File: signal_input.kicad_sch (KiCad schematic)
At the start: 48 parts, among them IC1 TXU0104QWBQARQ1, IC2 TXU0104QWBQARQ1, IC3 TXU0104QWBQARQ1, IC4 TXU0104QWBQARQ1, J4 6101XX249121_610108249121, J5 6101XX249121_610108249121, J6 6101XX249121_610108249121, J7 6101XX249121_610108249121

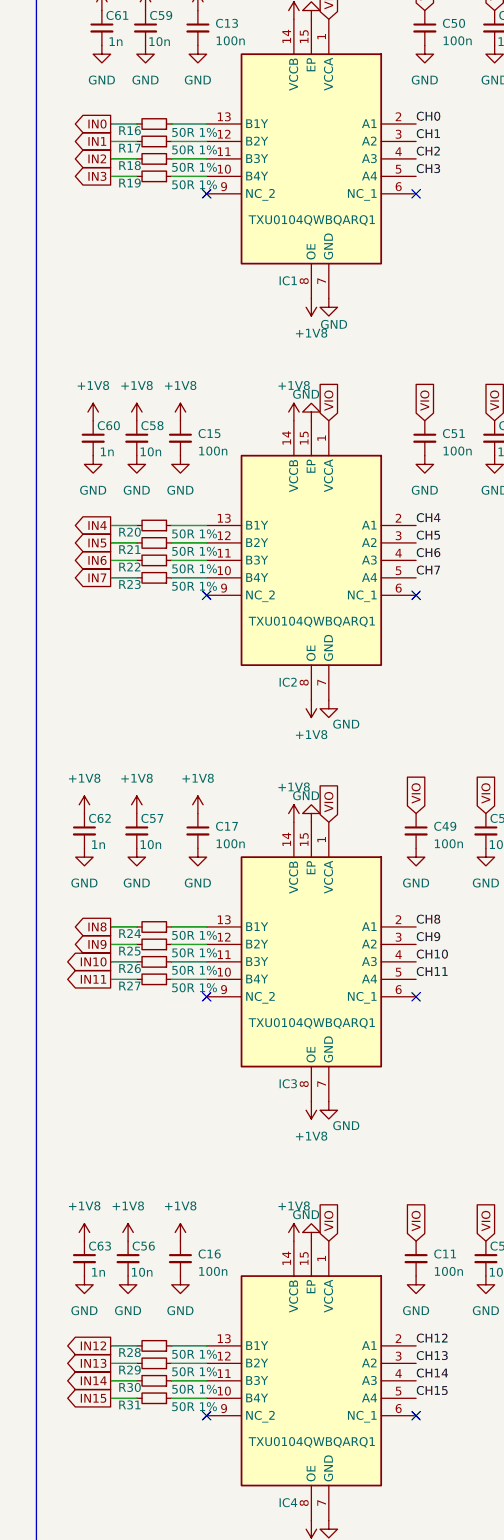
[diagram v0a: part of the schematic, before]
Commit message: implement all SML review nits
hopefully
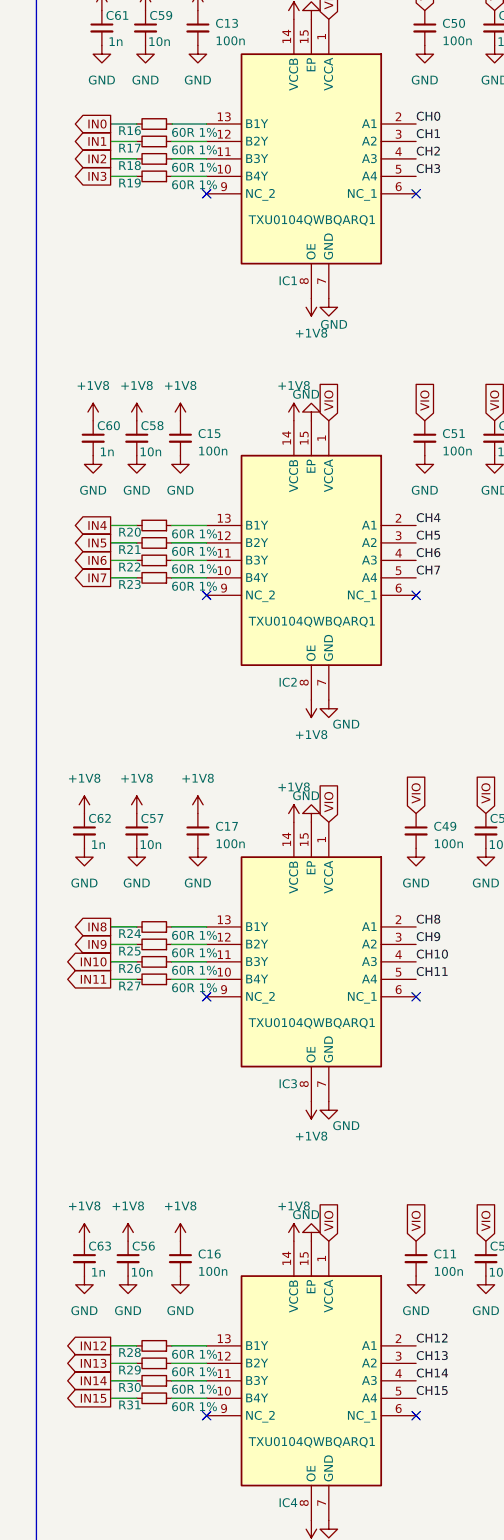
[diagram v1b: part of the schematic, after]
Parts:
- R16, R17, R18, R19, R20, R21, R22, R23, R24, R25, R26, R27, R28, R29, R30, R31: value 50R 1% -> 60R 1%; footprint Resistor_SMD:R_0201_0603Metric -> logic_analyzer:R_0201_0603Metric_input
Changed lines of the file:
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@@
 		(polyline
 			(pts
-				(xy 50.8 144.78) (xy 190.5 144.78) (xy 190.5 200.66) (xy 50.8 200.66)
+				(xy 50.8 27.94) (xy 190.5 27.94) (xy 190.5 83.82) (xy 50.8 83.82)
 			)
 			(stroke
@@
 		(polyline
 			(pts
-				(xy 50.8 27.94) (xy 190.5 27.94) (xy 190.5 83.82) (xy 50.8 83.82)
+				(xy 50.8 144.78) (xy 190.5 144.78) (xy 190.5 200.66) (xy 50.8 200.66)
 			)
 			(stroke
@@
 			)
 		)
-		(property "Value" "50R 1%"
+		(property "Value" "60R 1%"
 			(at 71.882 115.57 90)
 			(effects
@@
 			)
 		)
-		(property "Footprint" "Resistor_SMD:R_0201_0603Metric"
+		(property "Footprint" "logic_analyzer:R_0201_0603Metric_input"
 			(at 66.04 114.3 0)
 			(effects
@@
 			)
 		)
-		(property "Value" "50R 1%"
+		(property "Value" "60R 1%"
 			(at 71.882 229.87 90)
 			(effects
@@
 			)
 		)
-		(property "Footprint" "Resistor_SMD:R_0201_0603Metric"
+		(property "Footprint" "logic_analyzer:R_0201_0603Metric_input"
 			(at 66.04 228.6 0)
 			(effects
@@
 			)
 		)
-		(property "Value" "50R 1%"
+		(property "Value" "60R 1%"
 			(at 71.882 171.45 90)
 			(effects
@@
 			)
 		)
-		(property "Footprint" "Resistor_SMD:R_0201_0603Metric"
+		(property "Footprint" "logic_analyzer:R_0201_0603Metric_input"
 			(at 66.04 170.18 0)
 			(effects
@@
 			)
 		)
-		(property "Value" "50R 1%"
+		(property "Value" "60R 1%"
 			(at 71.882 234.95 90)
 			(effects
@@
 			)
 		)
-		(property "Footprint" "Resistor_SMD:R_0201_0603Metric"
+		(property "Footprint" "logic_analyzer:R_0201_0603Metric_input"
 			(at 66.04 233.68 0)
 			(effects
@@
 			)
 		)
-		(property "Value" "50R 1%"
+		(property "Value" "60R 1%"
 			(at 71.882 173.99 90)
 			(effects
@@
 			)
 		)
-		(property "Footprint" "Resistor_SMD:R_0201_0603Metric"
+		(property "Footprint" "logic_analyzer:R_0201_0603Metric_input"
 			(at 66.04 172.72 0)
 			(effects
@@
 			)
 		)
-		(property "Value" "50R 1%"
+		(property "Value" "60R 1%"
 			(at 71.882 176.53 90)
 			(effects
@@
 			)
 		)
-		(property "Footprint" "Resistor_SMD:R_0201_0603Metric"
+		(property "Footprint" "logic_analyzer:R_0201_0603Metric_input"
 			(at 66.04 175.26 0)
 			(effects
@@
 			)
 		)
-		(property "Value" "50R 1%"
+		(property "Value" "60R 1%"
 			(at 71.882 113.03 90)
 			(effects
@@
 			)
 		)
-		(property "Footprint" "Resistor_SMD:R_0201_0603Metric"
+		(property "Footprint" "logic_analyzer:R_0201_0603Metric_input"
 			(at 66.04 111.76 0)
 			(effects
@@
 			)
 		)
-		(property "Value" "50R 1%"
+		(property "Value" "60R 1%"
 			(at 71.882 59.69 90)
 			(effects
@@
 			)
 		)
-		(property "Footprint" "Resistor_SMD:R_0201_0603Metric"
+		(property "Footprint" "logic_analyzer:R_0201_0603Metric_input"
 			(at 66.04 58.42 0)
 			(effects
@@
 			)
 		)
-		(property "Value" "50R 1%"
+		(property "Value" "60R 1%"
 			(at 71.882 168.91 90)
 			(effects
@@
 			)
 		)
-		(property "Footprint" "Resistor_SMD:R_0201_0603Metric"
+		(property "Footprint" "logic_analyzer:R_0201_0603Metric_input"
 			(at 66.04 167.64 0)
 			(effects
@@
 			)
 		)
-		(property "Value" "50R 1%"
+		(property "Value" "60R 1%"
 			(at 71.882 54.61 90)
 			(effects
@@
 			)
 		)
-		(property "Footprint" "Resistor_SMD:R_0201_0603Metric"
+		(property "Footprint" "logic_analyzer:R_0201_0603Metric_input"
 			(at 66.04 53.34 0)
 			(effects
@@
 			)
 		)
-		(property "Value" "50R 1%"
+		(property "Value" "60R 1%"
 			(at 71.882 110.49 90)
 			(effects
@@
 			)
 		)
-		(property "Footprint" "Resistor_SMD:R_0201_0603Metric"
+		(property "Footprint" "logic_analyzer:R_0201_0603Metric_input"
 			(at 66.04 109.22 0)
 			(effects
@@
 			)
 		)
-		(property "Value" "50R 1%"
+		(property "Value" "60R 1%"
 			(at 71.882 52.07 90)
 			(effects
@@
 			)
 		)
-		(property "Footprint" "Resistor_SMD:R_0201_0603Metric"
+		(property "Footprint" "logic_analyzer:R_0201_0603Metric_input"
 			(at 66.04 50.8 0)
 			(effects
@@
 			)
 		)
-		(property "Value" "50R 1%"
+		(property "Value" "60R 1%"
 			(at 71.882 232.41 90)
 			(effects
@@
 			)
 		)
-		(property "Footprint" "Resistor_SMD:R_0201_0603Metric"
+		(property "Footprint" "logic_analyzer:R_0201_0603Metric_input"
 			(at 66.04 231.14 0)
 			(effects
@@
 			)
 		)
-		(property "Value" "50R 1%"
+		(property "Value" "60R 1%"
 			(at 71.882 118.11 90)
 			(effects
@@
 			)
 		)
-		(property "Footprint" "Resistor_SMD:R_0201_0603Metric"
+		(property "Footprint" "logic_analyzer:R_0201_0603Metric_input"
 			(at 66.04 116.84 0)
 			(effects
@@
 			)
 		)
-		(property "Value" "50R 1%"
+		(property "Value" "60R 1%"
 			(at 71.882 237.49 90)
 			(effects
@@
 			)
 		)
-		(property "Footprint" "Resistor_SMD:R_0201_0603Metric"
+		(property "Footprint" "logic_analyzer:R_0201_0603Metric_input"
 			(at 66.04 236.22 0)
 			(effects
@@
 			)
 		)
-		(property "Value" "50R 1%"
+		(property "Value" "60R 1%"
 			(at 71.882 57.15 90)
 			(effects
@@
 			)
 		)
-		(property "Footprint" "Resistor_SMD:R_0201_0603Metric"
+		(property "Footprint" "logic_analyzer:R_0201_0603Metric_input"
 			(at 66.04 55.88 0)
 			(effects
